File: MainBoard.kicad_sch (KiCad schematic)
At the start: 48 parts, among them SW1 SW_Push, SW10 SW_Push, SW11 SW_Push, SW12 SW_Push, SW13 SW_Push, SW14 SW_Push, SW15 SW_Push, SW16 SW_Push, SW17 SW_Push, SW18 SW_Push, SW19 SW_Push, SW2 SW_Push, SW20 SW_Push, SW21 SW_Push, SW22 SW_Push, SW23 SW_Push, SW3 SW_Push, SW4 SW_Push, SW5 SW_Push, SW6 SW_Push, SW7 SW_Push, SW8 SW_Push, SW9 SW_Push

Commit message: I/O Schematic rebuild from DRAFT by Nathann
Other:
- added sheet HumanInterfaceCircuitsII (HumanInterfaceCircuitsII.kicad_sch)
- added sheet IMU (IMU.kicad_sch)
- sheet BackLightsControl ports: added CargoCompLamp, DirIndicatorL, DirIndicatorR, DrivingBeam, RearDirLampL, RearDirLampR, RearFogLamp, RearPosLamp, RearSEL0, RearSEL1, RearSense, Reserved1, Reserved2, ReversingLamp, StopLamp, selG, selH, selI, selJ, selK, selL, ~{FaultRST}; removed none
- sheet FrontLightsControl ports: added AudibleWarn, DaytimeLamp, DrivingBeamLamp, FrontDirLampL, FrontDirLampR, FrontOutSEL0, FrontOutSEL1, FrontPosLamp, FrontSense, PassingBeamLamp, Reserved3, selA, selB, selC, selD, ~{FaultRST}; removed none
- sheet MCU ports: added ACCELERATOR_AN, AUX_AN, AUX_PAS_A, AUX_PAS_B, AudibleWarn, BreakLeft_SW, BreakRight_SW, CargoCompLamp, DaytimeLamp, DirIndicatorL, DirIndicatorR, DrivingBeam, DrivingBeamLamp, FrontDirLampL, FrontDirLampR, FrontOutSEL0, FrontOutSEL1, FrontPosLamp, FrontSense, PAS_A, PAS_B, PassingBeamLamp, REGEN_AN, RearDirLampL, RearDirLampR, RearFogLamp, RearPosLamp, RearSEL0, RearSEL1, RearSense, Reserved1, Reserved2, Reserved3, ReversingLamp, Seat_SW, SideDirLampL, SideDirLampR, SideMarkLampL, SideMarkLampR, SideSEL0, SideSEL1, SideSense, StopLamp, TORQUE_AN, TORQUE_PAS_A, TORQUE_PAS_B, Trunk_SW, selA, selB, selC, selD, selE, selF, selG, selH, selI, selJ, selK, selL, ~{FaultRST}; removed none
- sheet PowertrainInterface ports: added AUX_AN, AUX_PAS_A, AUX_PAS_B, TORQUE_AN, TORQUE_PAS_A, TORQUE_PAS_B; removed none
- sheet SideIndicatorLightsControl ports: added SideDirLampL, SideDirLampR, SideMarkLampL, SideMarkLampR, SideSEL0, SideSEL1, SideSense, selE, selF, ~{FaultRST}; removed none
- moved on the sheet: FID1, FID2, FID3, FID4, FID5, FID6, H1, H2, H3, H4, H5, H6

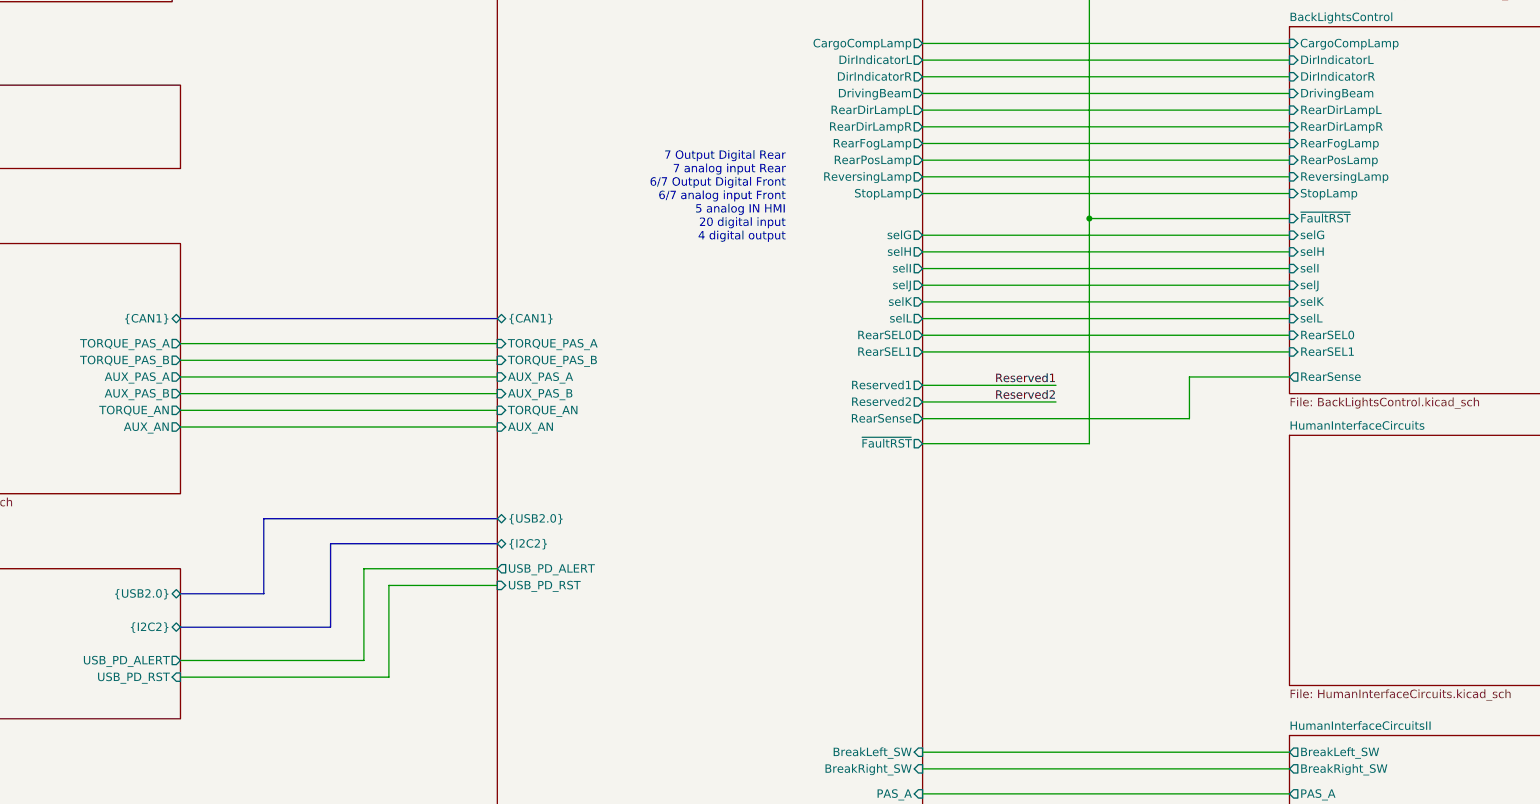
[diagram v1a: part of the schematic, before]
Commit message: integration of commodo signals to design
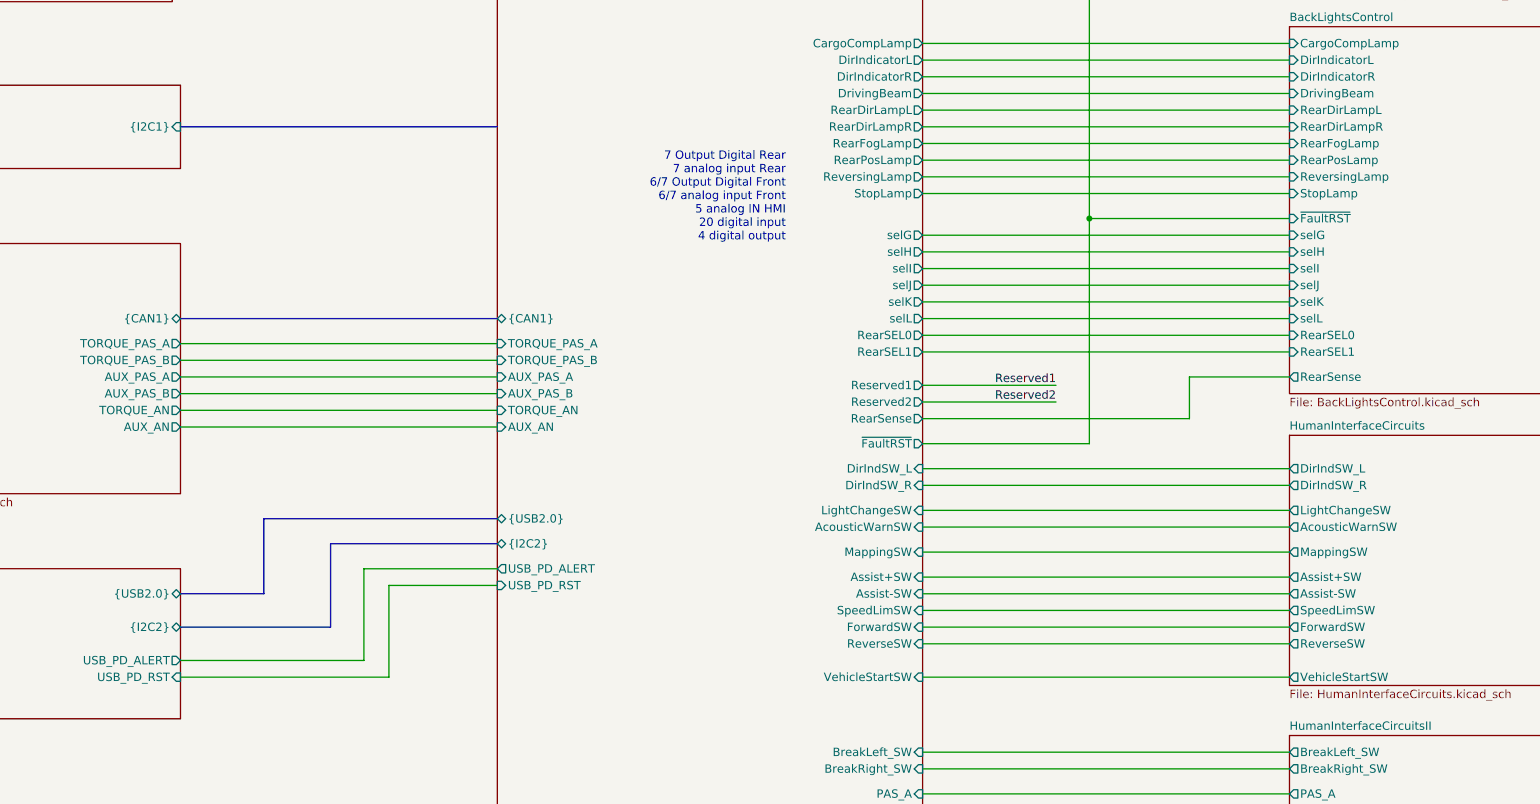
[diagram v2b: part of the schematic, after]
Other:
- sheet HumanInterfaceCircuits ports: added AcousticWarnSW, Assist+SW, Assist-SW, DirIndSW_L, DirIndSW_R, ForwardSW, LightChangeSW, MappingSW, ReverseSW, SpeedLimSW, VehicleStartSW; removed none
- sheet IMU ports: added {I2C1}; removed none
- sheet MCU ports: added AcousticWarnSW, Assist+SW, Assist-SW, DirIndSW_L, DirIndSW_R, ForwardSW, LightChangeSW, MappingSW, ReverseSW, SpeedLimSW, VehicleStartSW; removed none

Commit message: IMU block implementation
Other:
- sheet IMU ports: added ~{INT_ACC}; removed none
- sheet MCU ports: added {I2C1}, ~{INT_ACC}; removed none
- note removed: "7 Output Digital Rear 7 analog input Rear 6/7 Output Digital Front 6/7 analog input Front 5 analog IN HMI 20 digital input 4 digital output"
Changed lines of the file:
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@@
 	(text "Silixcon key IO"
 		(exclude_from_sim no)
-		(at 67.31 153.67 0)
+		(at 72.644 158.242 0)
 		(effects
 			(font
@@
 	(text "STM32H723"
 		(exclude_from_sim no)
-		(at 180.594 48.26 0)
+		(at 195.834 141.986 90)
 		(effects
 			(font
-				(size 1.27 1.27)
+				(size 5 5)
 			)
 		)
@@
 	(text "BMS CAN"
 		(exclude_from_sim no)
-		(at 69.088 150.622 0)
+		(at 69.596 155.448 0)
 		(effects
 			(font
@@
 	(text "Silixcon CAN"
 		(exclude_from_sim no)
-		(at 69.088 147.828 0)
+		(at 71.374 152.4 0)
 		(effects
 			(font
@@
 		)
 	)
-	(text "7 Output Digital Rear\n7 analog input Rear\n6/7 Output Digital Front\n6/7 analog input Front\n5 analog IN HMI\n20 digital input\n4 digital output"
-		(exclude_from_sim no)
-		(at 206.502 130.048 0)
-		(effects
-			(font
-				(size 1.27 1.27)
-			)
-			(justify right)
-		)
-	)
 	(text "12V"
 		(exclude_from_sim no)
@@
 		)
 	)
+	(wire
+		(pts
+			(xy 114.3 121.92) (xy 162.56 121.92)
+		)
+		(stroke
+			(width 0)
+			(type default)
+		)
+	)
 	(polyline
 		(pts
@@
 			)
 		)
+		(pin "~{INT_ACC}" output
+			(at 114.3 121.92 0)
+			(effects
+				(font
+					(size 1.27 1.27)
+				)
+				(justify right)
+			)
+		)
 		(instances
 			(project "MainBoard"
@@
 			)
 		)
+		(pin "{I2C1}" input
+			(at 162.56 119.38 180)
+			(effects
+				(font
+					(size 1.27 1.27)
+				)
+				(justify left)
+			)
+		)
+		(pin "~{INT_ACC}" input
+			(at 162.56 121.92 180)
+			(effects
+				(font
+					(size 1.27 1.27)
+				)
+				(justify left)
+			)
+		)

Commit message: EMI/EMC meassures implementation + VCU panel interface block
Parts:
- removed BZ1, BZ2: Buzzer, symbol Device:Buzzer
- removed D1, D10, D11, D2, D6, D7, D8, D9, docD5: LED, symbol Device:LED
- removed RV1, RV2: R_Potentiometer, symbol Device:R_Potentiometer
- removed SW1, SW10, SW11, SW12, SW13, SW14, SW15, SW16, SW17, SW18, SW19, SW2, SW20, SW21, SW22, SW23, SW3, SW4, SW5, SW6, SW7, SW8, SW9: SW_Push, symbol Switch:SW_Push
- FID1, FID2, FID3, FID4, FID5, FID6: symbol Mechanical:Fiducial -> VELION_VCU_Library:Fiducial
- H1, H2, H3, H4, H5, H6: symbol Mechanical:MountingHole -> VELION_VCU_Library:MountingHole
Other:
- removed sheet BMSinterface
- added sheet VCU_PanelInterface (VCU_PanelInterface.kicad_sch)
- sheet MCU ports: added FogLight_LED, FogLight_SW; removed none
- note added: "3-axis magnetometer MEMS"
- note added: "6-axis accelerometer MEMS"
- note added: "pressure + temp MEMS"
- note removed: "Assist + Assist - Reverse Forward speed limiter setpoint warning on/off ? GND"
- note removed: "Beware, different GND..."
- note removed: "Blinker Left Blinker Left Sequential Reverse light VCC T2 Brake T2 Fog light Blinker Right Blinker Right Sequential GND"
- note removed: "Blinker Left Side Light Left VCC E6C SW+ E6C SW- E6C Side Light Right Blinker Right Horn GND"
- note removed: "BrightstarTW A1 Vcc Blink GND"
- note removed: "BrightstarTW E6C Vcc (DRL) SW (shorting the sw SW wire switch between GND the mode DRL -> PASSING <-> DRIVING )"
- note removed: "BrightstarTW T2 Vcc (license plate + Pos) brake Vcc GND"
- note removed: "DK370"
- note removed: "PAS Front"
- note removed: "Speed limiter -> Mode switch, Assist <-> Speed limtier ?"
- note removed: "Throttle"
- note removed: "Torque rear"
- note removed: "VCC GND S1 S2 Torque"
- note removed: "VDS blinker + beam tell tale"
- note removed: "beam horn blinker L blinker R GND"
- note removed: "bonus for speed limiter"
- note removed: "https://ebikes.ca/resources/theory/pedal-assist.html"
- note removed: "left brake"
- note removed: "pedal regen"
- note removed: "regen"
- note removed: "right brake"
- note removed: "seat sensor"
